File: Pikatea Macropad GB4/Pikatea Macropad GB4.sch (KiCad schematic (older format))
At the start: 30 parts, among them J1 AVR-ISP-6, J2 USB_B_Mini, J3 Conn_01x03_Male, J4 Conn_01x03_Male, J5 Conn_01x03_Male, J6 Conn_01x06_Male, J7 Conn_01x03_Male, SW1 SW_DPST, SW2 Rotary_Encoder_Switch, U1 ATMEGA32U4-EP, X1 16MHz

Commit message: update GB4
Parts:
- added D2, D3, D4, D5, D6, D7: APA-106-F5, Pikatea:TONYU-DY-S352818-RGBC, symbol LED:APA-106-F5
- D1: footprint LED_THT:LED_D5.0mm-4_RGB -> Pikatea:TONYU-DY-S352818-RGBC
- MX1, MX2, MX3, MX4, MX5: footprint MX_Only:MXOnly-1U -> MX_Only:MXOnly-1U-NoLED
- U1: footprint Package_QFP:LQFP-44_10x10mm_P0.8mm -> Package_DFN_QFN:QFN-44-1EP_7x7mm_P0.5mm_EP5.15x5.15mm_ThermalVias
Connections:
- net at D1.1 (DO): now also D2.4 (DI)
- new net: D2.1 (DO), D3.4 (DI)
- new net: D3.1 (DO), D4.4 (DI)
- new net: D4.1 (DO), D5.4 (DI)
- new net: D5.1 (DO), D6.4 (DI)
- new net: D6.1 (DO), D7.4 (DI)
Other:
- moved on the sheet: D1
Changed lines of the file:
@@
 F 0 "U1" H 7075 6581 50  0000 C CNN
 F 1 "ATMEGA32U4-EP" H 7075 6490 50  0000 C CNN
-F 2 "Package_QFP:LQFP-44_10x10mm_P0.8mm" H 7100 4600 50  0001 C CIN
+F 2 "Package_DFN_QFN:QFN-44-1EP_7x7mm_P0.5mm_EP5.15x5.15mm_ThermalVias" H 7100 4600 50  0001 C CIN
 F 3 "" H 8200 5700 50  0001 C CNN
 	1    7100 4600
@@
 F 0 "MX1" H 7382 2074 60  0000 C CNN
 F 1 "MX-LED" H 7382 2000 20  0000 C CNN
-F 2 "MX_Only:MXOnly-1U" H 6675 1825 60  0001 C CNN
+F 2 "MX_Only:MXOnly-1U-NoLED" H 6675 1825 60  0001 C CNN
 F 3 "" H 6675 1825 60  0001 C CNN
 	1    7300 1850
@@
 F 0 "MX2" H 7832 2074 60  0000 C CNN
 F 1 "MX-LED" H 7832 2000 20  0000 C CNN
-F 2 "MX_Only:MXOnly-1U" H 7125 1825 60  0001 C CNN
+F 2 "MX_Only:MXOnly-1U-NoLED" H 7125 1825 60  0001 C CNN
 F 3 "" H 7125 1825 60  0001 C CNN
 	1    7750 1850
@@
 F 0 "MX3" H 8282 2074 60  0000 C CNN
 F 1 "MX-LED" H 8282 2000 20  0000 C CNN
-F 2 "MX_Only:MXOnly-1U" H 7575 1825 60  0001 C CNN
+F 2 "MX_Only:MXOnly-1U-NoLED" H 7575 1825 60  0001 C CNN
 F 3 "" H 7575 1825 60  0001 C CNN
 	1    8200 1850
@@
 F 0 "MX4" H 8732 2074 60  0000 C CNN
 F 1 "MX-LED" H 8732 2000 20  0000 C CNN
-F 2 "MX_Only:MXOnly-1U" H 8025 1825 60  0001 C CNN
+F 2 "MX_Only:MXOnly-1U-NoLED" H 8025 1825 60  0001 C CNN
 F 3 "" H 8025 1825 60  0001 C CNN
 	1    8650 1850
@@
 F 0 "MX5" H 9182 2074 60  0000 C CNN
 F 1 "MX-LED" H 9182 2000 20  0000 C CNN
-F 2 "MX_Only:MXOnly-1U" H 8475 1825 60  0001 C CNN
+F 2 "MX_Only:MXOnly-1U-NoLED" H 8475 1825 60  0001 C CNN
 F 3 "" H 8475 1825 60  0001 C CNN
 	1    9100 1850
@@
 L LED:APA-106-F5 D1
 U 1 1 61FC7D80
-P 1500 2750
-F 0 "D1" H 1844 2796 50  0000 L CNN
-F 1 "APA-106-F5" H 1844 2705 50  0000 L CNN
-F 2 "LED_THT:LED_D5.0mm-4_RGB" H 1550 2450 50  0001 L TNN
-F 3 "https://cdn.sparkfun.com/datasheets/Components/LED/COM-12877.pdf" H 1600 2375 50  0001 L TNN
-	1    1500 2750
-	1    0    0    -1
-$EndComp
+P 900 2600
+F 0 "D1" H 1244 2646 50  0000 L CNN
+F 1 "APA-106-F5" H 1244 2555 50  0000 L CNN
+F 2 "Pikatea:TONYU-DY-S352818-RGBC" H 950 2300 50  0001 L TNN
+F 3 "https://cdn.sparkfun.com/datasheets/Components/LED/COM-12877.pdf" H 1000 2225 50  0001 L TNN
+	1    900  2600
+	1    0    0    -1
+$EndComp
+$Comp
+L LED:APA-106-F5 D2
+U 1 1 61FFAAD7
+P 1500 2600
+F 0 "D2" H 1844 2646 50  0000 L CNN
+F 1 "APA-106-F5" H 1844 2555 50  0000 L CNN
+F 2 "Pikatea:TONYU-DY-S352818-RGBC" H 1550 2300 50  0001 L TNN
+F 3 "https://cdn.sparkfun.com/datasheets/Components/LED/COM-12877.pdf" H 1600 2225 50  0001 L TNN
+	1    1500 2600
+	1    0    0    -1
+$EndComp
+$Comp
+L LED:APA-106-F5 D3
+U 1 1 61FFB6F5
+P 2100 2600
+F 0 "D3" H 2444 2646 50  0000 L CNN
+F 1 "APA-106-F5" H 2444 2555 50  0000 L CNN
+F 2 "Pikatea:TONYU-DY-S352818-RGBC" H 2150 2300 50  0001 L TNN
+F 3 "https://cdn.sparkfun.com/datasheets/Components/LED/COM-12877.pdf" H 2200 2225 50  0001 L TNN
+	1    2100 2600
+	1    0    0    -1
+$EndComp
+$Comp
+L LED:APA-106-F5 D4
+U 1 1 61FFBE3A
+P 2700 2600
+F 0 "D4" H 3044 2646 50  0000 L CNN
+F 1 "APA-106-F5" H 3044 2555 50  0000 L CNN
+F 2 "Pikatea:TONYU-DY-S352818-RGBC" H 2750 2300 50  0001 L TNN
+F 3 "https://cdn.sparkfun.com/datasheets/Components/LED/COM-12877.pdf" H 2800 2225 50  0001 L TNN
+	1    2700 2600
+	1    0    0    -1
+$EndComp
+$Comp
+L LED:APA-106-F5 D5
+U 1 1 61FFC4C6
+P 3300 2600
+F 0 "D5" H 3644 2646 50  0000 L CNN
+F 1 "APA-106-F5" H 3644 2555 50  0000 L CNN
+F 2 "Pikatea:TONYU-DY-S352818-RGBC" H 3350 2300 50  0001 L TNN
+F 3 "https://cdn.sparkfun.com/datasheets/Components/LED/COM-12877.pdf" H 3400 2225 50  0001 L TNN
+	1    3300 2600
+	1    0    0    -1
+$EndComp
+$Comp
+L LED:APA-106-F5 D6
+U 1 1 61FFCE25
+P 3900 2600
+F 0 "D6" H 4244 2646 50  0000 L CNN
+F 1 "APA-106-F5" H 4244 2555 50  0000 L CNN
+F 2 "Pikatea:TONYU-DY-S352818-RGBC" H 3950 2300 50  0001 L TNN
+F 3 "https://cdn.sparkfun.com/datasheets/Components/LED/COM-12877.pdf" H 4000 2225 50  0001 L TNN
+	1    3900 2600
+	1    0    0    -1
+$EndComp
+$Comp
+L LED:APA-106-F5 D7
+U 1 1 61FFD683
+P 4500 2600
+F 0 "D7" H 4844 2646 50  0000 L CNN
+F 1 "APA-106-F5" H 4844 2555 50  0000 L CNN
+F 2 "Pikatea:TONYU-DY-S352818-RGBC" H 4550 2300 50  0001 L TNN
+F 3 "https://cdn.sparkfun.com/datasheets/Components/LED/COM-12877.pdf" H 4600 2225 50  0001 L TNN
+	1    4500 2600
+	1    0    0    -1
+$EndComp

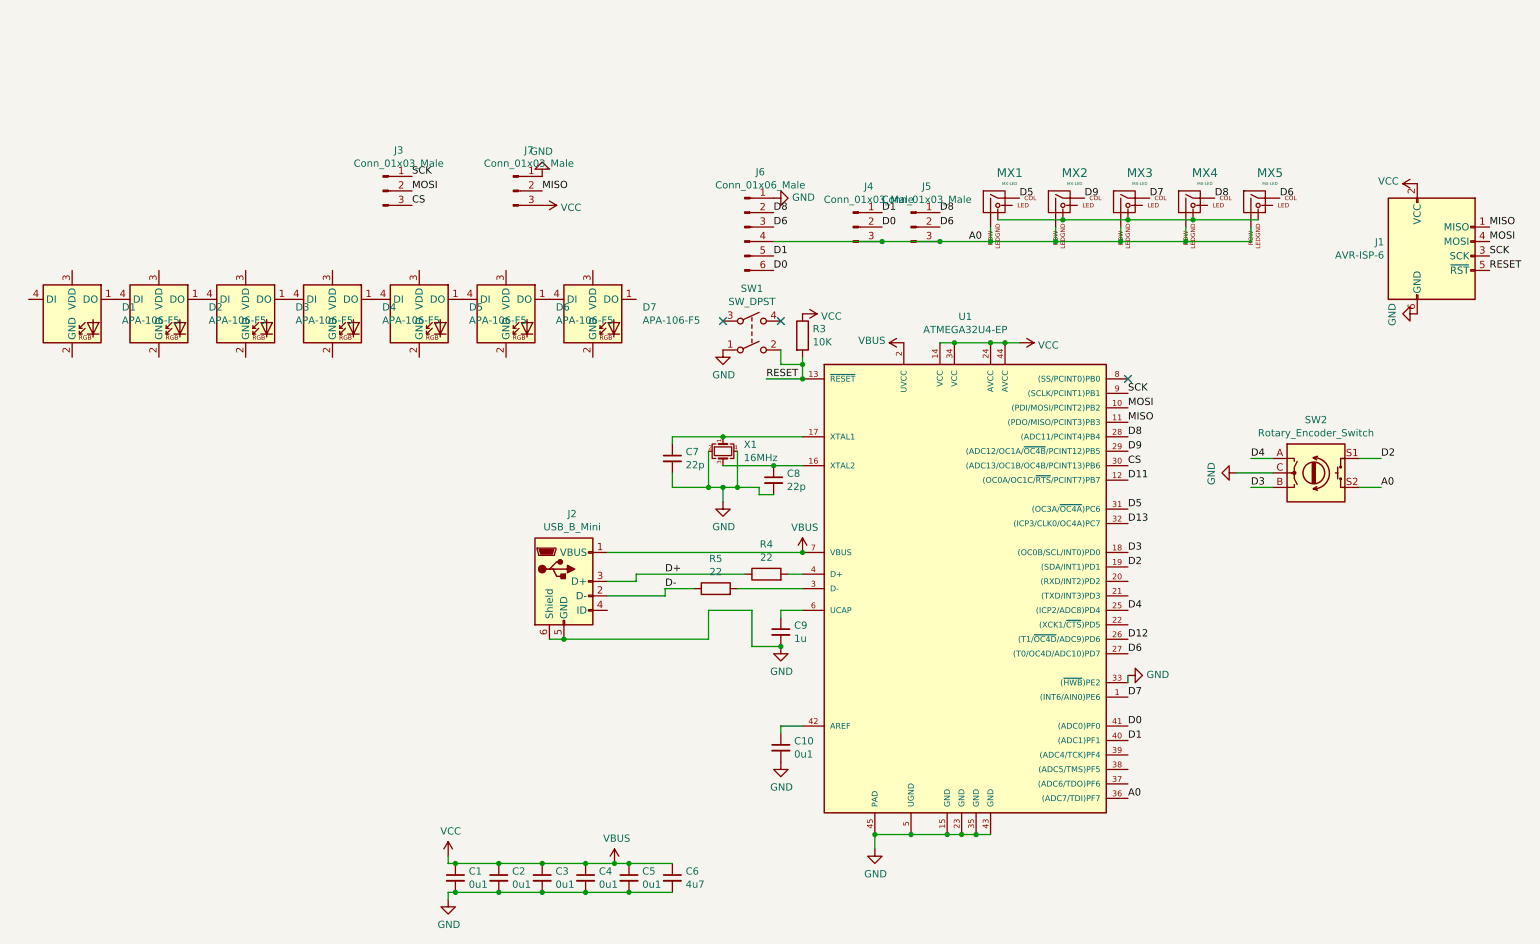
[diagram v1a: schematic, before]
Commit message: update r26 and gb4
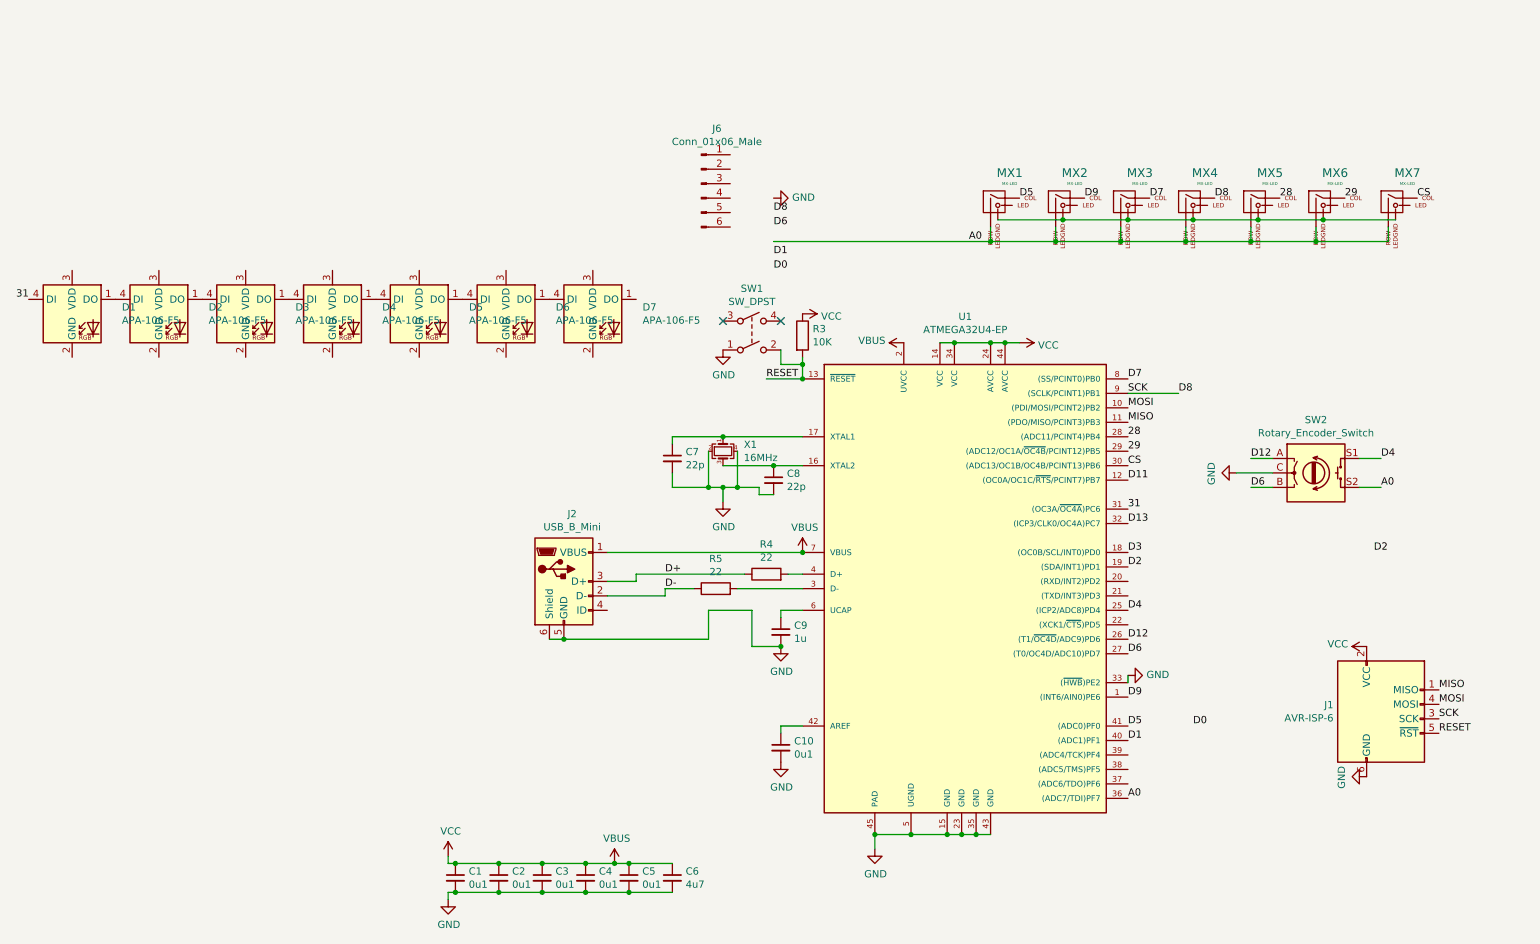
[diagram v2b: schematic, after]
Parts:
- removed J3, J4, J5, J7: Conn_01x03_Male, Connector_PinHeader_2.54mm:PinHeader_1x03_P2.54mm_Vertical, symbol Connector:Conn_01x03_Male
- added MX6, MX7: MX-LED, MX_Only:MXOnly-1U-NoLED, symbol MX_Alps_Hybrid:MX-LED
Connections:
- net SCK is gone; now on net D8: J1.3 (SCK), U1.9 ((SCLK/PCINT1)PB1)
- net A0: now also MX6.2 (ROW), MX7.2 (ROW); no longer J6.4 (Pin_4)
- net CS: now also MX7.1 (COL)
- net D0: no longer J6.6 (Pin_6), U1.41 ((ADC0)PF0)
- net D1: no longer J6.5 (Pin_5)
- net D12: now also SW2.A
- net D2: no longer SW2.S1
- net D3: no longer SW2.B
- net D4: now also SW2.S1; no longer SW2.A
- net D5: now also U1.41 ((ADC0)PF0); no longer U1.31 ((OC3A/~OC4A~)PC6)
- net D6: now also SW2.B; no longer J6.3 (Pin_3), MX5.1 (COL)
- net D7: now also U1.8 ((SS/PCINT0)PB0); no longer U1.1 ((INT6/AIN0)PE6)
- net D8: no longer J6.2 (Pin_2), U1.28 ((ADC11/PCINT4)PB4)
- net D9: now also U1.1 ((INT6/AIN0)PE6); no longer U1.29 ((ADC12/OC1A/~OC4B~/PCINT12)PB5)
- net GND: no longer J6.1 (Pin_1)
- net at MX1.4 (LEDGND), MX2.4 (LEDGND), MX3.4 (LEDGND)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: now also MX6.4 (LEDGND), MX7.4 (LEDGND)
- net 31: now reaches D1.4 (DI)
- net 31: now also U1.31 ((OC3A/~OC4A~)PC6)
- new net 28: MX5.1 (COL), U1.28 ((ADC11/PCINT4)PB4)
- new net 29: MX6.1 (COL), U1.29 ((ADC12/OC1A/~OC4B~/PCINT12)PB5)
- no-connect marks 3 -> 2
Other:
- moved on the sheet: J1, J6
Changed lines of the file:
@@
 Text Label 7900 1800 0    50   ~ 0
 D9
-Text Label 9250 1800 0    50   ~ 0
-D6
 Text Label 7450 1800 0    50   ~ 0
 D5
@@
 	0    -1   -1   0
 $EndComp
-NoConn ~ 8200 3050
 $Comp
 L Device:C_Small C1
@@
 Wire Wire Line
 	4750 6600 4450 6600
-Text Label 8200 5250 0    50   ~ 0
+Text Label 8200 3050 0    50   ~ 0
 D7
 Text Label 8200 5950 0    50   ~ 0
 A0
-Text Label 8200 3950 0    50   ~ 0
+Text Label 8200 5450 0    50   ~ 0
 D5
 Text Label 8200 3650 0    50   ~ 0
@@
 Wire Wire Line
 	8200 5150 8200 5100
-Text Label 8200 3550 0    50   ~ 0
+Text Label 8200 5250 0    50   ~ 0
 D9
-Text Label 8200 3450 0    50   ~ 0
+Text Label 8550 3150 0    50   ~ 0
 D8
 Text Label 8200 4950 0    50   ~ 0
@@
 	1    0    0    -1
 $EndComp
-Text Label 9950 3600 0    50   ~ 0
+Text Label 9900 4250 0    50   ~ 0
 D2
 Text Label 9950 3800 0    50   ~ 0
 A0
-Text Label 9050 3600 0    50   ~ 0
+Text Label 9950 3600 0    50   ~ 0
 D4
-Text Label 9050 3800 0    50   ~ 0
-D3
 $Comp
 L power:GND #PWR0115
@@
 	1    0    0    -1
 $EndComp
-Text Label 10700 2000 0    50   ~ 0
+Text Label 10350 5200 0    50   ~ 0
 MISO
-Text Label 10700 2100 0    50   ~ 0
+Text Label 10350 5300 0    50   ~ 0
 MOSI
-Text Label 10700 2200 0    50   ~ 0
+Text Label 10350 5400 0    50   ~ 0
 SCK
-Text Label 10700 2300 0    50   ~ 0
+Text Label 10350 5500 0    50   ~ 0
 RESET
 $Comp
 L power:GND #PWR0117
 U 1 1 600979DD
-P 10200 2600
-F 0 "#PWR0117" H 10200 2350 50  0001 C CNN
-F 1 "GND" H 10205 2427 50  0000 C CNN
-F 2 "" H 10200 2600 50  0001 C CNN
-F 3 "" H 10200 2600 50  0001 C CNN
-	1    10200 2600
+P 9850 5800
+F 0 "#PWR0117" H 9850 5550 50  0001 C CNN
+F 1 "GND" H 9855 5627 50  0000 C CNN
+F 2 "" H 9850 5800 50  0001 C CNN
+F 3 "" H 9850 5800 50  0001 C CNN
+	1    9850 5800
 	0    1    1    0
 $EndComp
@@
 L power:VCC #PWR0118
 U 1 1 60098DB5
-P 10200 1700
-F 0 "#PWR0118" H 10200 1550 50  0001 C CNN
-F 1 "VCC" V 10217 1828 50  0000 L CNN
-F 2 "" H 10200 1700 50  0001 C CNN
-F 3 "" H 10200 1700 50  0001 C CNN
-	1    10200 1700
+P 9850 4900
+F 0 "#PWR0118" H 9850 4750 50  0001 C CNN
+F 1 "VCC" V 9867 5028 50  0000 L CNN
+F 2 "" H 9850 4900 50  0001 C CNN
+F 3 "" H 9850 4900 50  0001 C CNN
+	1    9850 4900
 	0    -1   -1   0
 $EndComp
@@
 Connection ~ 5800 4900
 Connection ~ 5950 4250
-Wire Wire Line
-	6500 2100 6900 2100
-Text Label 6500 2000 0    50   ~ 0
-D0
-Text Label 6500 1900 0    50   ~ 0
-D1
 Text Label 8200 3750 0    50   ~ 0
 D11
 Text Label 8200 4050 0    50   ~ 0
 D13
-Text Label 8200 5450 0    50   ~ 0
+Text Label 8650 5450 0    50   ~ 0
 D0
 Text Label 8200 5550 0    50   ~ 0
 D1
-Text Label 8200 4850 0    50   ~ 0
-D12
 Wire Wire Line
 	8150 2100 8600 2100
@@
 Text Label 8800 1800 0    50   ~ 0
 D8
-$Comp
-L Connector:Conn_01x03_Male J4
-U 1 1 601A4B28
-P 6300 2000
-F 0 "J4" H 6408 2281 50  0000 C CNN
-F 1 "Conn_01x03_Male" H 6408 2190 50  0000 C CNN
-F 2 "Connector_PinHeader_2.54mm:PinHeader_1x03_P2.54mm_Vertical" H 6300 2000 50  0001 C CNN
-F 3 "~" H 6300 2000 50  0001 C CNN
-	1    6300 2000
-	1    0    0    -1
-$EndComp
-$Comp
-L Connector:Conn_01x03_Male J5
-U 1 1 601F09E4
-P 6700 2000
-F 0 "J5" H 6808 2281 50  0000 C CNN
-F 1 "Conn_01x03_Male" H 6808 2190 50  0000 C CNN
-F 2 "Connector_PinHeader_2.54mm:PinHeader_1x03_P2.54mm_Vertical" H 6700 2000 50  0001 C CNN
-F 3 "~" H 6700 2000 50  0001 C CNN
-	1    6700 2000
-	1    0    0    -1
-$EndComp
-Connection ~ 6900 2100
-Wire Wire Line
-	6900 2100 7250 2100
-Text Label 6900 1900 0    50   ~ 0
-D8
-Text Label 6900 2000 0    50   ~ 0
-D6
 Text Label 5750 1900 0    50   ~ 0
 D8
 Text Label 5750 2000 0    50   ~ 0
 D6
-Wire Wire Line
-	5750 2100 6500 2100
-Connection ~ 6500 2100
 $Comp
 L power:GND #PWR0101
@@
 Connection ~ 8650 1950
 $Comp
-L Connector:Conn_01x03_Male J3
-U 1 1 60614122
-P 3050 1750
-F 0 "J3" H 3158 2031 50  0000 C CNN
-F 1 "Conn_01x03_Male" H 3158 1940 50  0000 C CNN
-F 2 "Connector_PinHeader_2.54mm:PinHeader_1x03_P2.54mm_Vertical" H 3050 1750 50  0001 C CNN
-F 3 "~" H 3050 1750 50  0001 C CNN
-	1    3050 1750
-	1    0    0    -1
-$EndComp
-$Comp
-L Connector:Conn_01x03_Male J7
-U 1 1 606149C4
-P 3950 1750
-F 0 "J7" H 4058 2031 50  0000 C CNN
-F 1 "Conn_01x03_Male" H 4058 1940 50  0000 C CNN
-F 2 "Connector_PinHeader_2.54mm:PinHeader_1x03_P2.54mm_Vertical" H 3950 1750 50  0001 C CNN
-F 3 "~" H 3950 1750 50  0001 C CNN
-	1    3950 1750
-	1    0    0    -1
-$EndComp
-Text Label 3250 1650 0    50   ~ 0
-SCK
-Text Label 3250 1750 0    50   ~ 0
-MOSI
-Text Label 3250 1850 0    50   ~ 0
-CS
-Text Label 4150 1750 0    50   ~ 0
-MISO
-$Comp
-L power:GND #PWR0102
-U 1 1 6061DB34
-P 4150 1650
-F 0 "#PWR0102" H 4150 1400 50  0001 C CNN
-F 1 "GND" H 4155 1477 50  0000 C CNN
-F 2 "" H 4150 1650 50  0001 C CNN
-F 3 "" H 4150 1650 50  0001 C CNN
-	1    4150 1650
-	-1   0    0    1
-$EndComp
-$Comp
-L power:VCC #PWR0114
-U 1 1 606210F2
-P 4150 1850
-F 0 "#PWR0114" H 4150 1700 50  0001 C CNN
-F 1 "VCC" V 4165 1978 50  0000 L CNN
-F 2 "" H 4150 1850 50  0001 C CNN
-F 3 "" H 4150 1850 50  0001 C CNN
-	1    4150 1850
-	0    1    1    0
-$EndComp
-$Comp
 L Connector:AVR-ISP-6 J1
 U 1 1 6089E8EE
-P 10300 2200
-F 0 "J1" H 9971 2296 50  0000 R CNN
-F 1 "AVR-ISP-6" H 9971 2205 50  0000 R CNN
-F 2 "keyboard_parts:AVR_ICSP_3x2" V 10050 2250 50  0001 C CNN
-F 3 " ~" H 9025 1650 50  0001 C CNN
-	1    10300 2200
+P 9950 5400
+F 0 "J1" H 9621 5496 50  0000 R CNN
+F 1 "AVR-ISP-6" H 9621 5405 50  0000 R CNN
+F 2 "keyboard_parts:AVR_ICSP_3x2" V 9700 5450 50  0001 C CNN
+F 3 " ~" H 8675 4850 50  0001 C CNN
+	1    9950 5400
 	1    0    0    -1
 $EndComp
@@
 L Connector:Conn_01x06_Male J6
 U 1 1 60A0116B
-P 5550 2000
-F 0 "J6" H 5658 2381 50  0000 C CNN
-F 1 "Conn_01x06_Male" H 5658 2290 50  0000 C CNN
-F 2 "Pikatea Macropad Encoder Side Mount:Breakaway-Throughole" H 5550 2000 50  0001 C CNN
-F 3 "~" H 5550 2000 50  0001 C CNN
-	1    5550 2000
+P 5250 1700
+F 0 "J6" H 5358 2081 50  0000 C CNN
+F 1 "Conn_01x06_Male" H 5358 1990 50  0000 C CNN
+F 2 "Pikatea Macropad Encoder Side Mount:Breakaway-Throughole" H 5250 1700 50  0001 C CNN
+F 3 "~" H 5250 1700 50  0001 C CNN
+	1    5250 1700
 	1    0    0    -1
 $EndComp
@@
 	1    0    0    -1
 $EndComp
+Wire Wire Line
+	5750 2100 7250 2100
+Wire Wire Line
+	8200 3150 8550 3150
+Text Label 8200 4850 0    50   ~ 0
+D12
+Text Label 9050 3600 0    50   ~ 0
+D12
+Text Label 9050 3800 0    50   ~ 0
+D6
+Text Label 8200 3450 0    50   ~ 0
+28
+Text Label 9250 1800 0    50   ~ 0
+28
+Text Label 8200 3950 0    50   ~ 0
+31
+Text Label 600  2500 2    50   ~ 0
+31
+$Comp
+L MX_Alps_Hybrid:MX-LED MX6
+U 1 1 620A6780
+P 9550 1850
+F 0 "MX6" H 9632 2074 60  0000 C CNN
+F 1 "MX-LED" H 9632 2000 20  0000 C CNN
+F 2 "MX_Only:MXOnly-1U-NoLED" H 8925 1825 60  0001 C CNN
+F 3 "" H 8925 1825 60  0001 C CNN
+	1    9550 1850
+	1    0    0    -1
+$EndComp
+$Comp
+L MX_Alps_Hybrid:MX-LED MX7
+U 1 1 620A6EAA
+P 10050 1850
+F 0 "MX7" H 10132 2074 60  0000 C CNN
+F 1 "MX-LED" H 10132 2000 20  0000 C CNN
+F 2 "MX_Only:MXOnly-1U-NoLED" H 9425 1825 60  0001 C CNN
+F 3 "" H 9425 1825 60  0001 C CNN
+	1    10050 1850
+	1    0    0    -1
+$EndComp
+Wire Wire Line
+	9050 2100 9500 2100
+Wire Wire Line
+	9500 2100 9500 2000
+Connection ~ 9050 2100
+Wire Wire Line
+	9500 2100 10000 2100
+Wire Wire Line
+	10000 2100 10000 2000
+Connection ~ 9500 2100
+Wire Wire Line
+	9100 1950 9550 1950
+Connection ~ 9100 1950
+Connection ~ 9550 1950
+Wire Wire Line
+	9550 1950 10050 1950
+Text Label 10200 1800 0    50   ~ 0
+CS
+Text Label 8200 3550 0    50   ~ 0
+29
+Text Label 9700 1800 0    50   ~ 0
+29
 $EndSCHEMATC

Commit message: Revision b of GB4
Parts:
- removed J6: Conn_01x06_Male, Pikatea Macropad Encoder Side Mount:Breakaway-Throughole, symbol Connector:Conn_01x06_Male
- added J3, J4: Conn_01x11_Female, Pikatea:Breakaway-Throughole-GB4, symbol Connector:Conn_01x11_Female
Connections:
- net 28: now also J3.5 (Pin_5)
- net 29: now also J3.4 (Pin_4), J4.3 (Pin_3)
- net A0: now also J3.1 (Pin_1), J4.1 (Pin_1)
- net CS: now also J3.3 (Pin_3), J4.2 (Pin_2)
- net D8: now also J3.6 (Pin_6)
- net GND: now also D1.2 (GND), D2.2 (GND), D3.2 (GND), D4.2 (GND), D5.2 (GND), D6.2 (GND), D7.2 (GND), J3.10 (Pin_10), J3.11 (Pin_11), J3.2 (Pin_2), J3.9 (Pin_9), J4.10 (Pin_10), J4.11 (Pin_11), J4.4 (Pin_4), J4.5 (Pin_5), J4.6 (Pin_6), J4.8 (Pin_8)
- net VBUS: now also D1.3 (VDD), D2.3 (VDD), D3.3 (VDD), D4.3 (VDD), D5.3 (VDD), D6.3 (VDD), D7.3 (VDD), J3.7 (Pin_7), J4.7 (Pin_7)
- net at D3.1 (DO), D4.4 (DI): now also J3.8 (Pin_8)
- net at D5.1 (DO), D6.4 (DI): now also J4.9 (Pin_9)
